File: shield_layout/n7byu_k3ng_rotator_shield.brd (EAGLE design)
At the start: 100 x 80 mm, 22 parts, among them J1 ARDUINO_R3_SHIELD

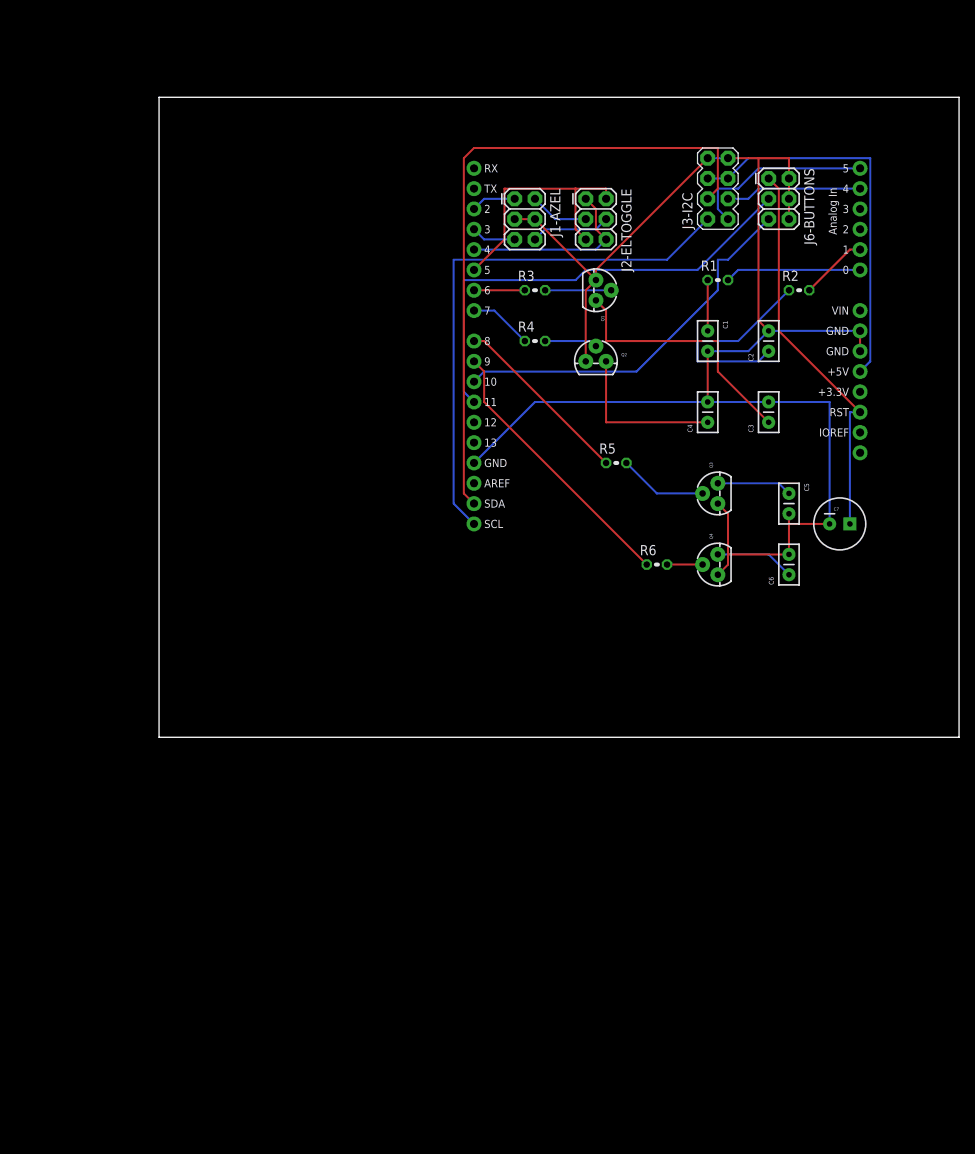
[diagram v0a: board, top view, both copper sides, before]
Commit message: switching back to separate headers. hopefully will be easier to route on the PCB
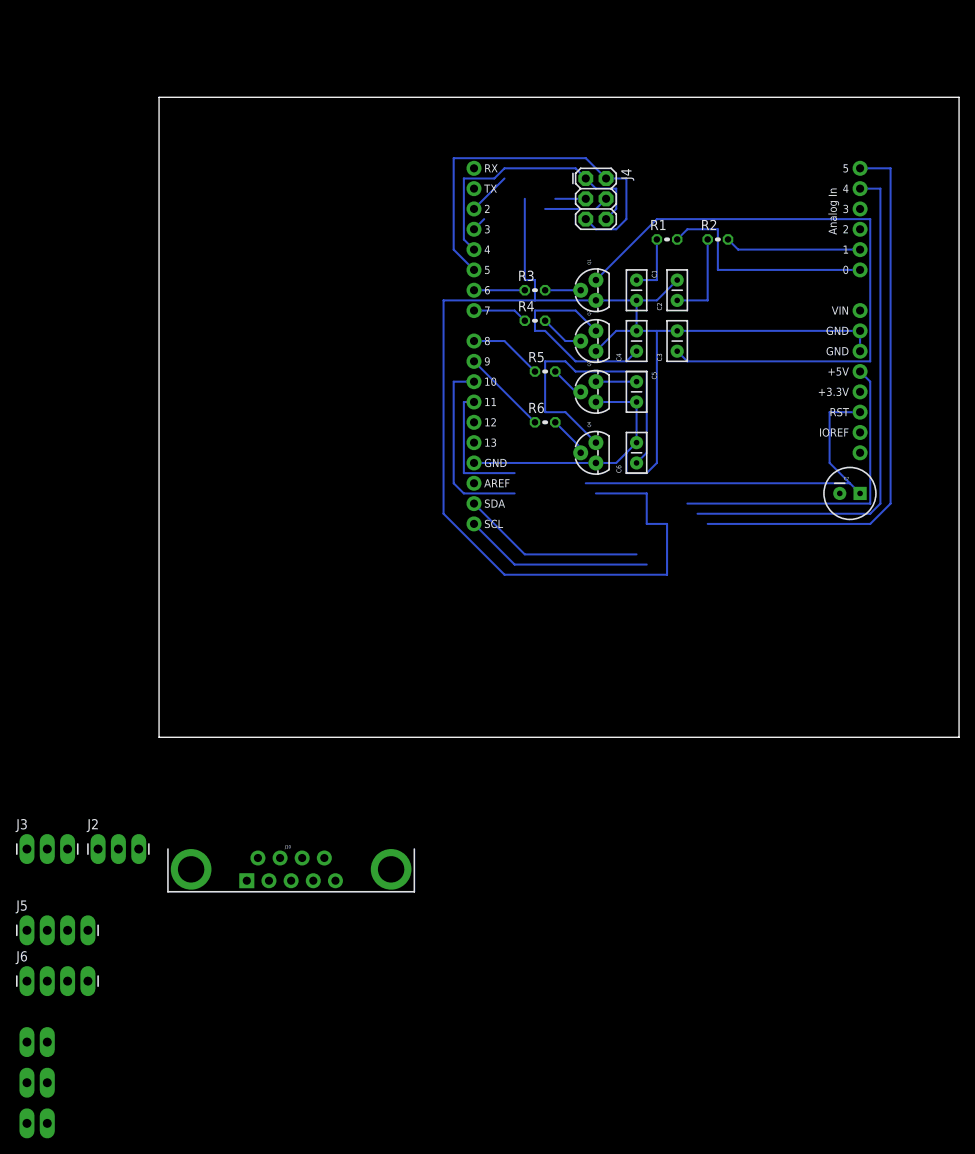
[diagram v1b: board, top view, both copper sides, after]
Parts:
- removed J1-AZEL, J2-ELTOGGLE, J6-BUTTONS: (no value), SparkFun-Connectors:2X3
- removed J3-I2C: (no value), SparkFun-Connectors:2X4
- added J10: ROTCABLE, SparkFun-Connectors:DB9
- added J2: EL, SparkFun-Connectors:1X03_LONGPADS
- added J3: AZ, SparkFun-Connectors:1X03_LONGPADS
- added J4: ELToggle, SparkFun-Connectors:2X3
- added J5: I2C-OLD, SparkFun-Connectors:1X04_LONGPADS
- added J6: I2C-NEW, SparkFun-Connectors:1X04_LONGPADS
- added J7: RST, SparkFun-Connectors:1X02_LONGPADS
- added J8: PARK, SparkFun-Connectors:1X02_LONGPADS
- added J9: STOP, SparkFun-Connectors:1X02_LONGPADS
- Q1, Q2, Q3, Q4: value (none) -> 2N3904
- moved C5 23.6 mm to (59.7, 44.5)
- moved C6 23.6 mm to (59.7, 34.3)
- moved R6 22.6 mm to (48.3, 39.4)
- moved Q4 20.7 mm to (54.6, 35.6)
- moved Q3 19.8 mm to (54.6, 43.2)
- moved C3 14.5 mm to (64.8, 48.3)
- moved R5 14.5 mm to (48.3, 45.7)
- moved C2 13.1 mm to (64.8, 54.6)
- moved C4 12.6 mm to (59.7, 48.3)
- moved R2 12.0 mm to (69.8, 62.2)
- moved C1 10.9 mm to (59.7, 57.1)
- moved R1 8.13 mm to (63.5, 62.2)
- moved C7 4.02 mm to (86.4, 30.5)
- moved Q2 2.54 mm to (54.6, 49.5), turned to 90 degrees
- moved R4 2.54 mm to (47.0, 52.1)
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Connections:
- removed net N$11: C5.1, Q3.3
- new net N$18: C5.1, J10.5, Q3.3
- net CCW-BUTTON: now also J3.1; no longer J1-AZEL.5
- net CW-BUTTON: now also J3.3; no longer J1-AZEL.1
- net GND: now also J10.8, J10.9, J2.2, J3.2, J5.1, J6.1, J7.2, J8.2, J9.2; no longer J1-AZEL.3, J1-AZEL.4, J3-I2C.7, J3-I2C.8, J6-BUTTONS.2, J6-BUTTONS.4, J6-BUTTONS.6
- net N$1: now also J10.6
- net N$10: now also J10.2
- net N$12: now also J10.3
- net N$13: now also J7.1; no longer J6-BUTTONS.1
- net N$14: now also J2.1, J4.4; no longer J1-AZEL.6, J2-ELTOGGLE.4
- net N$21: now also J2.3, J4.3; no longer J1-AZEL.2, J2-ELTOGGLE.3
- net N$23: now also J4.1, J4.6; no longer J2-ELTOGGLE.1, J2-ELTOGGLE.6
- net N$24: now also J4.2, J4.5; no longer J2-ELTOGGLE.2, J2-ELTOGGLE.5
- net N$25: now also J5.4; no longer J3-I2C.1
- net N$26: now also J5.2, J6.2; no longer J3-I2C.5, J3-I2C.6
- net N$27: now also J5.3; no longer J3-I2C.3
- net N$28: now also J9.1; no longer J6-BUTTONS.5
- net N$29: now also J6.3; no longer J3-I2C.4
- net N$31: now also J8.1; no longer J6-BUTTONS.3
- net N$32: now also J6.4; no longer J3-I2C.2
- net N$5: now also J10.1
- net N$9: now also J10.4
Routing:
- net N$29: track 82.9 -> 23.0 mm
- net N$27: track 17.0 -> 65.3 mm
- net N$9: track 32.4 -> 79.9 mm
- net N$25: track 23.2 -> 69.6 mm
- net N$32: track 67.9 -> 23.7 mm
- net N$31: track 58.1 -> 16.5 mm
- net N$12: track 9.94 -> 39.5 mm
- net N$28: track 47.5 -> 23.4 mm
- net N$19: track 34.3 -> 10.8 mm
- net N$24: track 32.6 -> 48.9 mm
- net N$5: track 26.0 -> 11.4 mm
- net N$17: track 22.8 -> 9.20 mm
- net GND: track 204.5 -> 216.4 mm
- net N$4: track 17.0 -> 28.5 mm
- net N$23: track 23.2 -> 34.4 mm
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
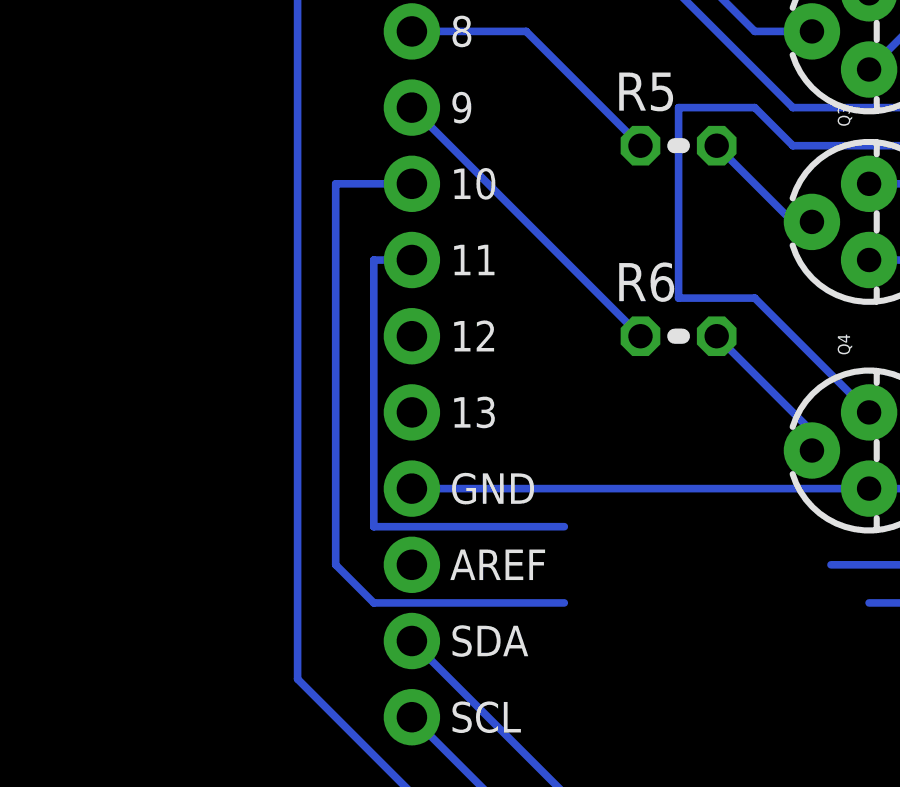
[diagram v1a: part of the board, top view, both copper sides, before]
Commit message: cleaning up schematic file after merge conflict
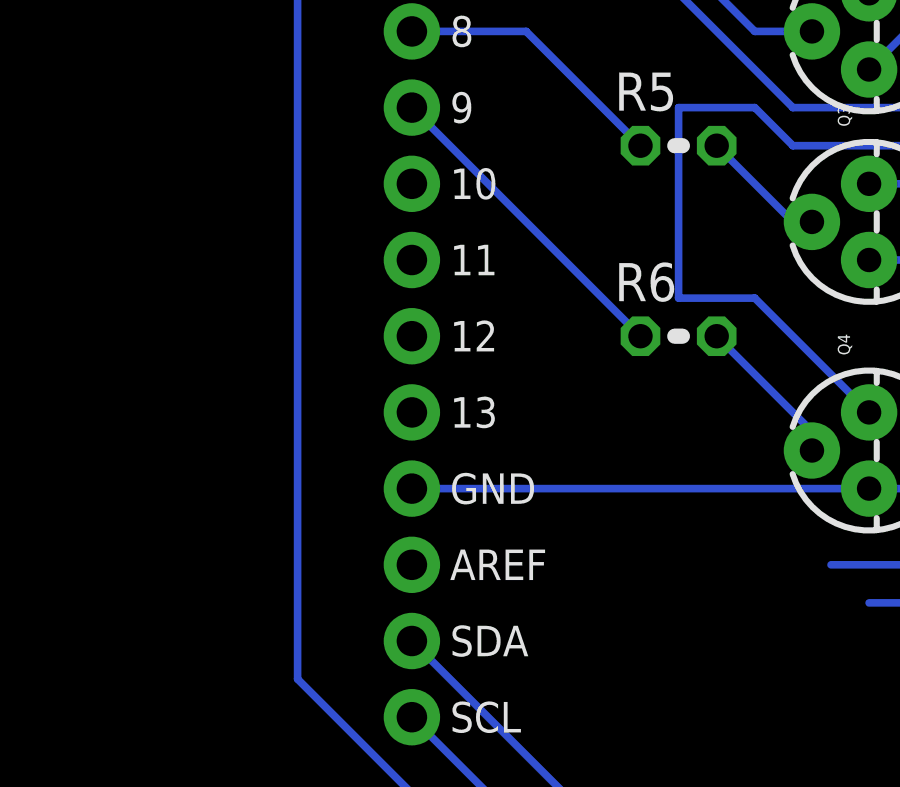
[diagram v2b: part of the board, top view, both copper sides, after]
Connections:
- removed net N$31: J1.D11, J8.1
- new net N$22: J1.A2, J9.1
- net N$28: now also J1.A3, J8.1; no longer J1.D10, J9.1
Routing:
- net N$28: track 23.4 -> 0.00 mm
- net N$31: track 16.5 -> 0.00 mm
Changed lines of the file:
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@@
 <wire x1="-8.89" y1="-24.13" x2="68.58" y2="26.67" width="0" layer="19" extent="16-16"/>
-</signal>
-<signal name="N$28">
-<contactref element="J1" pad="D10"/>
-<wire x1="38.1" y1="30.48" x2="44.45" y2="30.48" width="0.254" layer="16"/>
-<wire x1="36.83" y1="31.75" x2="38.1" y2="30.48" width="0.254" layer="16"/>
-<wire x1="36.83" y1="44.45" x2="36.83" y2="31.75" width="0.254" layer="16"/>
-<wire x1="39.37" y1="44.45" x2="36.83" y2="44.45" width="0.254" layer="16"/>
-<contactref element="J9" pad="1"/>
-<wire x1="-16.51" y1="-48.26" x2="38.1" y2="30.48" width="0" layer="19" extent="16-16"/>
-</signal>
-<signal name="N$31">
-<contactref element="J1" pad="D11"/>
-<wire x1="38.1" y1="33.02" x2="44.45" y2="33.02" width="0.254" layer="16"/>
-<wire x1="38.1" y1="41.91" x2="38.1" y2="33.02" width="0.254" layer="16"/>
-<wire x1="39.37" y1="41.91" x2="38.1" y2="41.91" width="0.254" layer="16"/>
-<contactref element="J8" pad="1"/>
-<wire x1="-16.51" y1="-43.18" x2="38.1" y2="33.02" width="0" layer="19" extent="16-16"/>
 </signal>
 <signal name="N$29">
@@
 <wire x1="22.05" y1="-17.93" x2="54.61" y2="44.45" width="0" layer="19" extent="1-1"/>
 </signal>
+<signal name="N$22">
+<contactref element="J1" pad="A2"/>
+<contactref element="J9" pad="1"/>
+<wire x1="-16.51" y1="-48.26" x2="87.63" y2="63.5" width="0" layer="19" extent="1-1"/>
+</signal>
+<signal name="N$28">
+<contactref element="J8" pad="1"/>
+<contactref element="J1" pad="A3"/>
+<wire x1="-16.51" y1="-43.18" x2="87.63" y2="66.04" width="0" layer="19" extent="1-1"/>
+</signal>
 </signals>

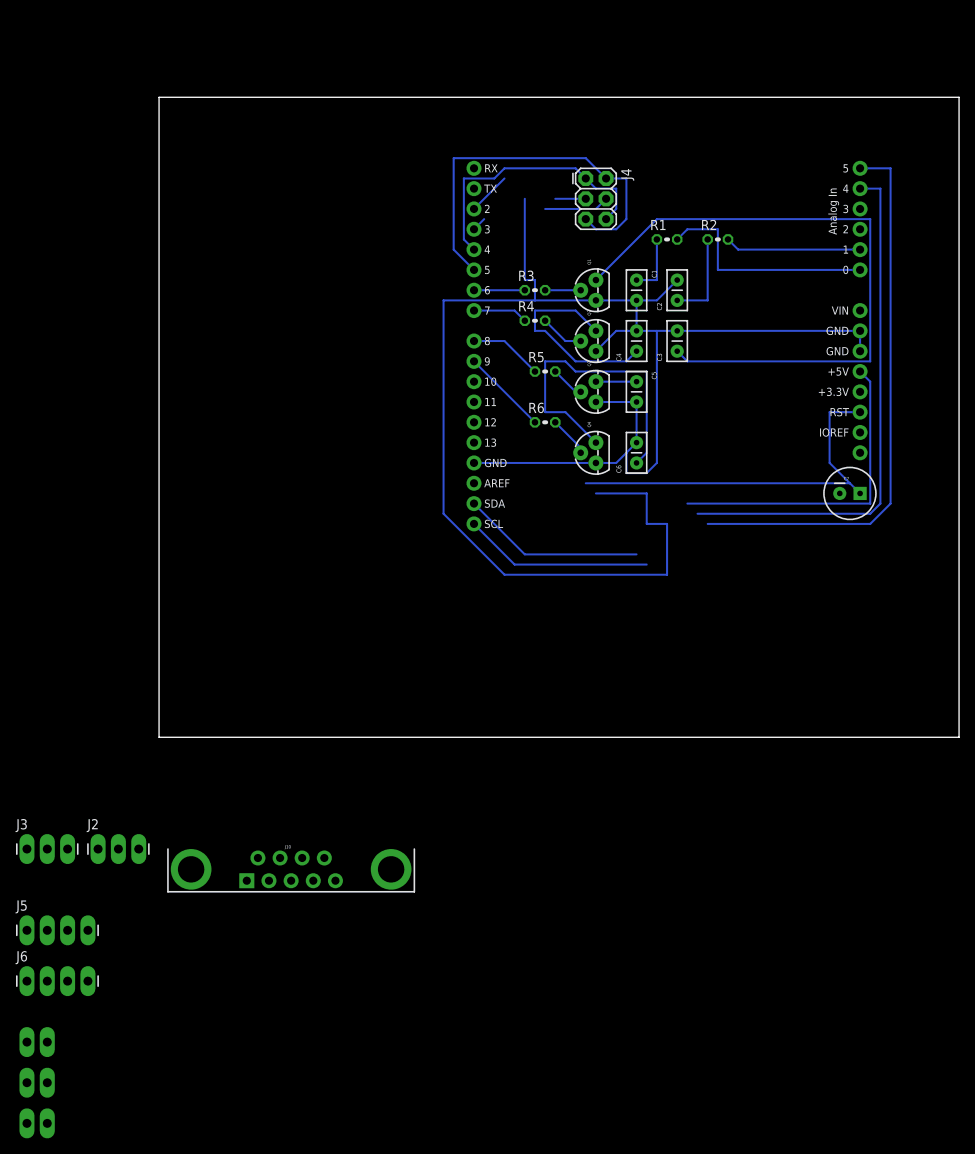
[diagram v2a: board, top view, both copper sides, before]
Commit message: another attempt at single-layer routing. not quite there yet
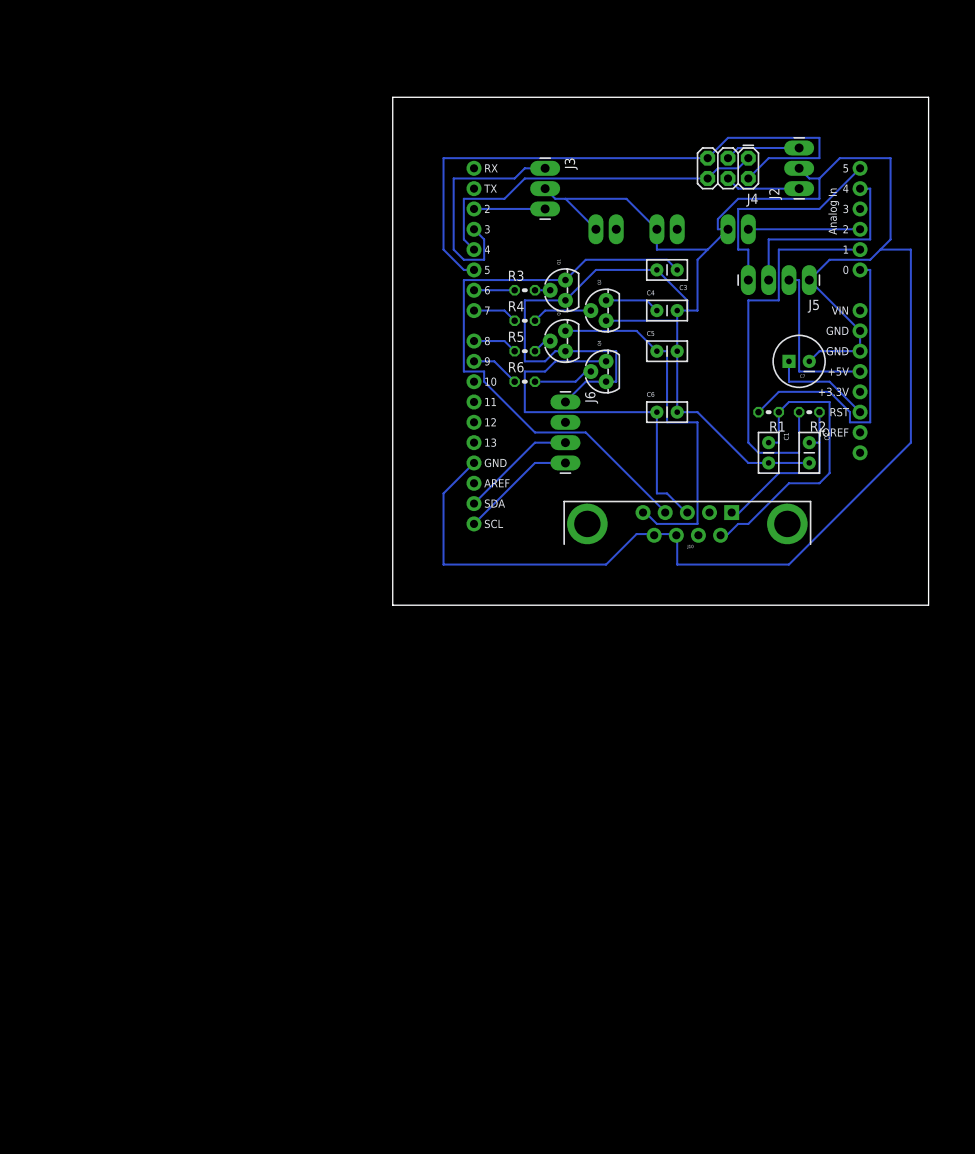
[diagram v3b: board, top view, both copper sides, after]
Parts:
- moved J9 143.6 mm to (73.7, 63.5), turned to 180 degrees
- moved J8 134.1 mm to (64.8, 63.5), turned to 180 degrees
- moved J5 127.2 mm to (81.3, 57.1), turned to 180 degrees
- moved J7 125.5 mm to (57.1, 63.5), turned to 180 degrees
- moved J2 120.4 mm to (80.0, 68.6), turned to 90 degrees
- moved J3 106.9 mm to (48.3, 71.1), turned to 270 degrees
- moved J6 98.8 mm to (50.8, 41.9), turned to 270 degrees
- moved J10 65.7 mm to (66.0, 26.7), turned to 180 degrees
- moved C1 26.2 mm to (76.2, 36.8)
- moved R1 25.0 mm to (76.2, 40.6), turned to 180 degrees
- moved R2 24.4 mm to (81.3, 40.6), turned to 180 degrees
- moved C2 24.3 mm to (81.3, 36.8), turned to 270 degrees
- moved J4 20.5 mm to (73.7, 72.4), turned to 180 degrees
- moved C7 17.7 mm to (80.0, 47.0), turned to 180 degrees
- moved Q4 10.2 mm to (55.9, 45.7)
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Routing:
- net GND: track 216.4 -> 326.1 mm
- net N$25: track 69.6 -> 27.5 mm
- net N$18: track 5.08 -> 46.5 mm
- net N$27: track 65.3 -> 25.4 mm
- net N$13: track 48.6 -> 13.0 mm
- net N$6: track 17.0 -> 50.1 mm
- net N$1: track 7.62 -> 37.6 mm
- net N$24: track 48.9 -> 76.8 mm
- net CCW-BUTTON: track 1.80 -> 29.5 mm
- net N$26: track 39.9 -> 20.3 mm
- net N$10: track 26.0 -> 6.88 mm
- net N$22: track 0.00 -> 14.0 mm
- net N$5: track 11.4 -> 22.0 mm
- net N$23: track 34.4 -> 44.5 mm
- net N$4: track 28.5 -> 37.7 mm
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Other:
- board size 100 x 80 mm -> 67 x 63.5 mm

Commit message: got it down to 3 jumpers on one layer. still working...
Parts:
- moved J7 29.2 mm to (81.3, 47.0), turned to 90 degrees
- moved C7 17.3 mm to (85.1, 30.5), turned to 270 degrees
- moved J6 16.9 mm to (47.0, 25.4), turned to 90 degrees
- moved C5 14.2 mm to (68.6, 35.6), turned to 180 degrees
- moved Q4 14.2 mm to (58.4, 31.8)
- moved C6 13.3 mm to (66.0, 27.9)
- moved J9 11.5 mm to (62.2, 64.8), turned to 270 degrees
- moved C4 10.9 mm to (66.0, 43.2)
- moved R1 10.2 mm to (74.9, 50.8), turned to 90 degrees
- moved Q3 10.2 mm to (50.8, 39.4)
- moved C3 9.67 mm to (68.6, 49.5)
- moved R2 7.41 mm to (77.5, 47.0), turned to 90 degrees
- moved J5 6.48 mm to (80.0, 63.5), turned to 270 degrees
- moved C1 6.35 mm to (76.2, 43.2)
- moved C2 6.35 mm to (81.3, 43.2)
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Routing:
- net N$9: track 73.5 -> 20.9 mm
- net N$10: track 6.88 -> 45.6 mm
- net N$18: track 46.5 -> 80.3 mm
- net N$1: track 37.6 -> 7.62 mm
- net N$28: track 0.00 -> 29.1 mm
- net N$6: track 50.1 -> 23.2 mm
- net N$26: track 20.3 -> 47.1 mm
- net N$4: track 37.7 -> 15.3 mm
- net CCW-BUTTON: track 29.5 -> 11.5 mm
- net CW-BUTTON: track 8.89 -> 26.8 mm
- net N$12: track 47.4 -> 32.5 mm
- net N$3: track 7.51 -> 22.0 mm
- net N$22: track 14.0 -> 0.00 mm
- net GND: track 326.1 -> 312.6 mm
- net N$5: track 22.0 -> 33.9 mm
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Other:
- board size 67 x 63.5 mm -> 100 x 90.2 mm
